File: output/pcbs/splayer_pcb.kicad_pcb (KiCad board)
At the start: 2 copper layers, 124.4 x 92.7 mm, 34 parts

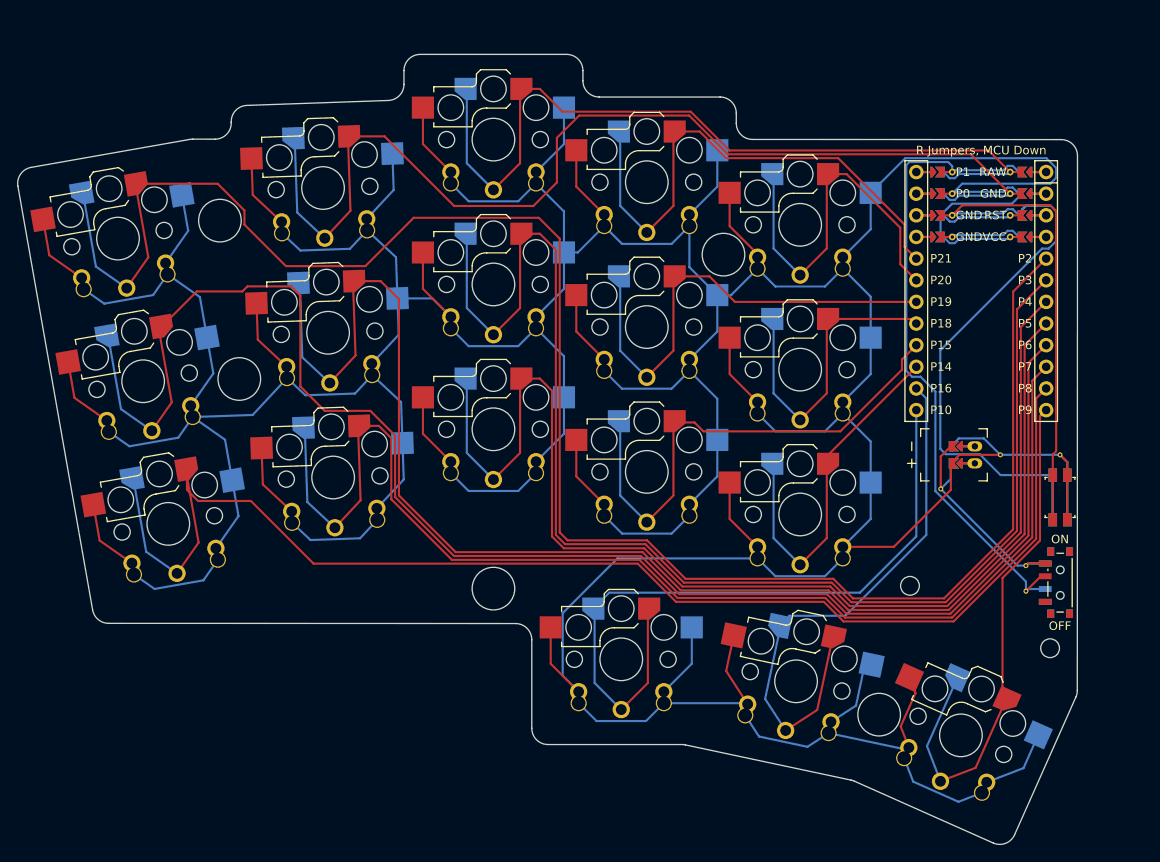
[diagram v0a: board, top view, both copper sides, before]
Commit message: designed a new plate case for the keyboard
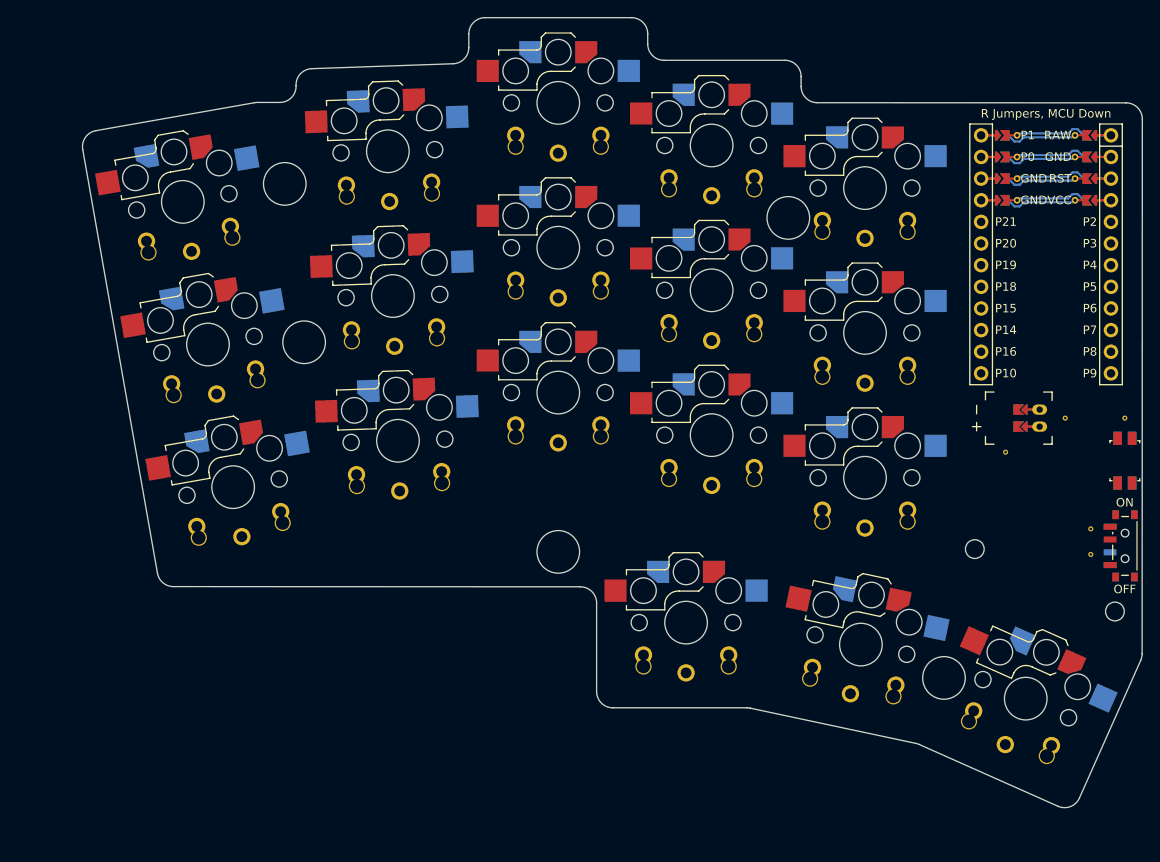
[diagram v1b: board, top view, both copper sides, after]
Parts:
- removed the REF** at (183.1, 100.2)
- removed the REF** at (193.1, 112.2)
- removed the REF** at (197.1, 96.2)
- removed the REF** at (190.1, 96.2)
- removed the REF** at (193.1, 109.2)
- added REF**: VIA-0.6mm, VIA-0.6mm, F.Cu at (204.7, 91.9)
- added REF**: VIA-0.6mm, VIA-0.6mm, F.Cu at (197.7, 91.9)
- added REF**: VIA-0.6mm, VIA-0.6mm, F.Cu at (200.7, 104.9)
- added REF**: VIA-0.6mm, VIA-0.6mm, F.Cu at (200.7, 107.9)
- added REF**: VIA-0.6mm, VIA-0.6mm, F.Cu at (190.7, 95.9)
- moved MH1 8.75 mm to (203.5, 114.6)
- moved S16 8.75 mm to (153.2, 115.9)
- moved S3 8.75 mm to (94.1, 66.5)
- moved PWR1 8.75 mm to (204.7, 106.9)
- moved S15 8.75 mm to (174.2, 64.9)
- moved S18 8.75 mm to (193.0, 124.8)
- moved MH2 8.75 mm to (187.1, 107.3)
- moved MH6 8.75 mm to (138.2, 107.6)
- moved MCU1 8.75 mm to (195.4, 71.4)
- moved S12 8.75 mm to (156.2, 59.9)
- moved S6 8.75 mm to (118.2, 60.6)
- moved S14 8.75 mm to (174.2, 81.9)
- moved S7 8.75 mm to (138.2, 88.9)
- moved S17 8.75 mm to (173.7, 118.5)
- moved S1 8.75 mm to (100.0, 100.0)
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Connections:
- S1 pad 2: GND -> P8
- S10 pad 2: GND -> P15
- S11 pad 2: GND -> P19
- S12 pad 2: GND -> P21
- S13 pad 2: GND -> P14
- S14 pad 2: GND -> P18
- S15 pad 2: GND -> P20
- S16 pad 2: GND -> P10
- S17 pad 2: GND -> P16
- S18 pad 2: GND -> P9
- S2 pad 2: GND -> P6
- S3 pad 2: GND -> P2
- S4 pad 2: GND -> P7
- S5 pad 2: GND -> P5
- S6 pad 2: GND -> P0
- S7 pad 2: GND -> P4
- S8 pad 2: GND -> P3
- S9 pad 2: GND -> P1
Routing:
- net GND: track 849.1 -> 0.00 mm
- net P2: track 212.1 -> 0.00 mm
- net P6: track 183.5 -> 0.00 mm
- net P5: track 164.0 -> 0.00 mm
- net P8: track 157.1 -> 0.00 mm
- net P3: track 156.4 -> 0.00 mm
- net P7: track 143.5 -> 0.00 mm
- net P4: track 138.0 -> 0.00 mm
- net P0: track 128.5 -> 0.00 mm
- net RST: track 127.8 -> 0.00 mm
- net (no net): track 0.00 -> 112.6 mm
- net P1: track 97.7 -> 0.00 mm
- net P10: track 82.7 -> 0.00 mm
- net RAW: track 78.1 -> 0.00 mm
- net P16: track 65.8 -> 0.00 mm
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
